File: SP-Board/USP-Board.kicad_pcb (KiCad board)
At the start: 2 copper layers, 55 x 55 mm, 8 parts, among them J10 RJ45, J11 RJ45, Q1 MMBT3906, U1 ADS1015IDGS

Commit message: Needs wires board layout 95%
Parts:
- added C1: C_Small, Capacitor_Tantalum_SMD:CP_EIA-1608-08_AVX-J_Pad1.25x1.05mm_HandSolder, B.Cu at (159.0, 107.0)
- added C2: 1uF, Capacitor_Tantalum_SMD:CP_EIA-1608-08_AVX-J_Pad1.25x1.05mm_HandSolder, B.Cu at (147.0, 95.0)
- added C3: 1uF, Capacitor_Tantalum_SMD:CP_EIA-1608-08_AVX-J_Pad1.25x1.05mm_HandSolder, B.Cu at (159.0, 98.0)
- added C4: 1uF, Capacitor_Tantalum_SMD:CP_EIA-1608-08_AVX-J_Pad1.25x1.05mm_HandSolder, B.Cu at (154.0, 98.0)
- added C5: 1uF, Capacitor_Tantalum_SMD:CP_EIA-1608-08_AVX-J_Pad1.25x1.05mm_HandSolder, B.Cu at (147.0, 89.8)
- added C6: 1uF, Capacitor_Tantalum_SMD:CP_EIA-1608-08_AVX-J_Pad1.25x1.05mm_HandSolder, B.Cu at (147.0, 85.0)
- added D1: LED, LED_SMD:LED_0603_1608Metric, F.Cu at (149.0, 110.0)
- added J1: Conn_01x02, 2.54mm_Pin_Headers:PinHeader_1x02_P2.54mm_Vertical, F.Cu at (136.0, 113.0)
- added J12: Conn_01x04, 2.54mm_Pin_Headers:PinHeader_1x04_P2.54mm_Vertical, F.Cu at (142.0, 92.0)
- added J2: Conn_01x02, 2.54mm_Pin_Headers:PinHeader_1x02_P2.54mm_Vertical, F.Cu at (136.0, 103.0)
- added J3: Conn_01x02, 2.54mm_Pin_Headers:PinHeader_1x02_P2.54mm_Vertical, F.Cu at (136.0, 108.0)
- added J4: Conn_01x02, 2.54mm_Pin_Headers:PinHeader_1x02_P2.54mm_Vertical, F.Cu at (136.0, 98.0)
- added J5: Conn_02x05_Odd_Even, Blue_ESC:Amphenol 98424-G52-10LF, F.Cu at (170.0, 89.0)
- added J6: Conn_01x03, 2.54mm_Pin_Headers:PinHeader_1x03_P2.54mm_Vertical, F.Cu at (182.0, 118.0)
- added J7: Conn_01x04, 2.54mm_Pin_Headers:PinHeader_1x04_P2.54mm_Vertical, F.Cu at (182.0, 106.0)
- added J8: Conn_01x03, 2.54mm_Pin_Headers:PinHeader_1x03_P2.54mm_Vertical, F.Cu at (177.0, 101.0)
- added J9: Conn_01x04, 2.54mm_Pin_Headers:PinHeader_1x04_P2.54mm_Vertical, F.Cu at (182.0, 111.0)
- added R1: 1k, Resistor_SMD:R_1206_3216Metric_Pad1.42x1.75mm_HandSolder, B.Cu at (142.0, 101.0)
- added R2: 27k, Resistor_SMD:R_1206_3216Metric_Pad1.42x1.75mm_HandSolder, B.Cu at (149.0, 101.0)
- added R3: 1k, Resistor_SMD:R_1206_3216Metric_Pad1.42x1.75mm_HandSolder, B.Cu at (142.0, 106.0)
- added R4: 240, Resistor_SMD:R_1206_3216Metric_Pad1.42x1.75mm_HandSolder, B.Cu at (142.0, 110.0)
- added U2: MAX232, Package_SO:SOIC-16_3.9x9.9mm_P1.27mm, B.Cu at (154.0, 90.0)
- Q1, U1: moved to B.Cu
- moved U1 14.3 mm to (159.0, 103.0), turned to 180 degrees
- moved Q1 8.41 mm to (149.0, 105.0), turned to 270 degrees
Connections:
- U1 pad 4: ANLG_Induction_SENS -> ANLG_HAL_SENS
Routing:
- net GND: track 0.00 -> 1.85 mm
- added copper zone on B.Cu, net GND

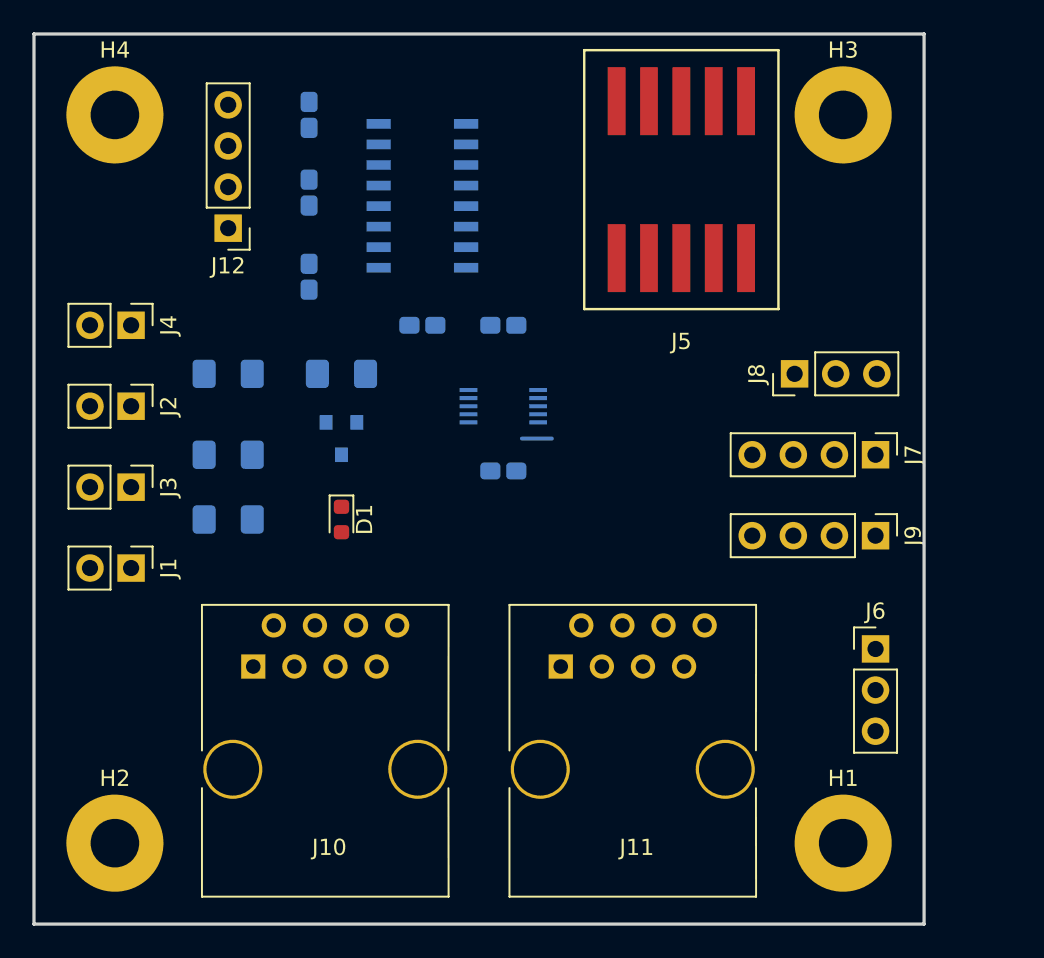
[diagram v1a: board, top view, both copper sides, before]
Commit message: added xt60
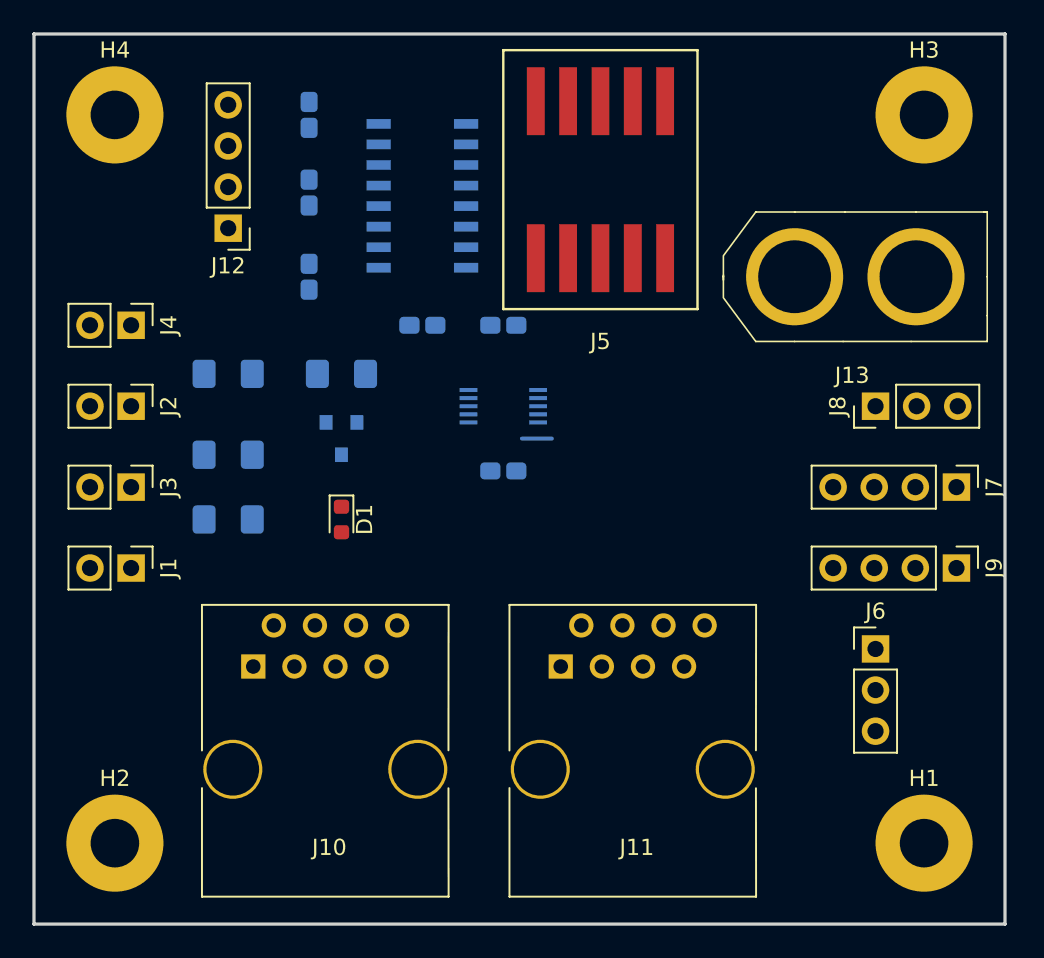
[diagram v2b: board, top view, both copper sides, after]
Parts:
- added J13: Conn_01x02, Blue_ESC:XT60, F.Cu at (177.0, 95.0)
- moved J7 5.39 mm to (187.0, 108.0)
- moved J8 5.39 mm to (182.0, 103.0)
- moved J9 5.39 mm to (187.0, 113.0)
- moved H1 5.00 mm to (185.0, 130.0)
- moved H3 5.00 mm to (185.0, 85.0)
- moved J5 5.00 mm to (165.0, 89.0)
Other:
- board size 55 x 55 mm -> 60 x 55 mm
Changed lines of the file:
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@@
     (tracks 1)
     (zones 0)
-    (modules 30)
+    (modules 31)
     (nets 43)
   )
@@
   )
   (module MountingHole:MountingHole_3mm_Pad (layer F.Cu)
-    (at 180 130)
+    (at 185 130)
     (descr "Mounting Hole 3mm")
     (tags "mounting hole 3mm")
@@
   )
   (module MountingHole:MountingHole_3mm_Pad (layer F.Cu)
-    (at 180 85)
+    (at 185 85)
     (descr "Mounting Hole 3mm")
     (tags "mounting hole 3mm")
@@
   )
   (module "Blue_ESC:Amphenol 98424-G52-10LF" (layer F.Cu)
-    (at 170 89)
+    (at 165 89)
     (fp_text reference J5 (at 0 10) (layer F.SilkS)
       (effects (font (size 1 1) (thickness 0.15)))
@@
   )
   (module 2.54mm_Pin_Headers:PinHeader_1x04_P2.54mm_Vertical (layer F.Cu)
-    (at 182 106 270)
+    (at 187 108 270)
     (descr "Through hole straight pin header, 1x04, 2.54mm pitch, single row")
     (tags "Through hole pin header THT 1x04 2.54mm single row")
@@
   )
   (module 2.54mm_Pin_Headers:PinHeader_1x03_P2.54mm_Vertical (layer F.Cu)
-    (at 177 101 90)
+    (at 182 103 90)
     (descr "Through hole straight pin header, 1x03, 2.54mm pitch, single row")
     (tags "Through hole pin header THT 1x03 2.54mm single row")
@@
   )
   (module 2.54mm_Pin_Headers:PinHeader_1x04_P2.54mm_Vertical (layer F.Cu)
-    (at 182 111 270)
+    (at 187 113 270)
     (descr "Through hole straight pin header, 1x04, 2.54mm pitch, single row")
     (tags "Through hole pin header THT 1x04 2.54mm single row")
@@
     )
   )
+  (module Blue_ESC:XT60 (layer F.Cu)
+    (at 177 95)
+    (fp_text reference J13 (at 3.556 6.096) (layer F.SilkS)
+      (effects (font (size 1 1) (thickness 0.15)))
+    )
+    (fp_text value Conn_01x02 (at 3.2 -5.9) (layer F.Fab)
+      (effects (font (size 1 1) (thickness 0.15)))
+    )
+    (fp_line (start 7.2 4) (end 11.9 4) (layer F.SilkS) (width 0.1))
+    (fp_line (start 11.9 4) (end 11.9 2.4) (layer F.SilkS) (width 0.1))
+    (fp_line (start 7.5 -4) (end 11.7 -4) (layer F.SilkS) (width 0.1))
+    (fp_line (start 11.7 -4) (end 11.8 -4) (layer F.SilkS) (width 0.1))
+    (fp_line (start 11.8 -4) (end 11.9 -4) (layer F.SilkS) (width 0.1))
+    (fp_line (start 11.9 -4) (end 11.9 0) (layer F.SilkS) (width 0.1))
+    (fp_line (start -2.4 4) (end -4.4 1.3) (layer F.SilkS) (width 0.1))
+    (fp_line (start -2.4 -4) (end -4.4 -1.3) (layer F.SilkS) (width 0.1))
+    (fp_line (start -4.4 0) (end -4.4 1.25) (layer F.SilkS) (width 0.1))
+    (fp_line (start -4.4 0) (end -4.4 -1.25) (layer F.SilkS) (width 0.1))
+    (fp_line (start 0 4) (end -2.4 4) (layer F.SilkS) (width 0.1))
+    (fp_line (start 3 4) (end 0 4) (layer F.SilkS) (width 0.1))
+    (fp_line (start 0 -4) (end -2.4 -4) (layer F.SilkS) (width 0.1))
+    (fp_line (start 3.1 -4) (end 0 -4) (layer F.SilkS) (width 0.1))
+    (fp_line (start -4.4 -0.1) (end -4.4 0.2) (layer F.SilkS) (width 0.1))
+    (fp_line (start 11.9 0) (end 11.9 2.4) (layer F.SilkS) (width 0.1))
+    (fp_line (start 7.5 -4) (end 3.1 -4) (layer F.SilkS) (width 0.1))
+    (fp_line (start 7.2 4) (end 3 4) (layer F.SilkS) (width 0.1))
+    (pad 1 thru_hole circle (at 0 0) (size 6 6) (drill 4.5) (layers *.Cu *.Mask F.SilkS)
+      (net 6 GND))
+    (pad 2 thru_hole circle (at 7.5 0) (size 6 6) (drill 4.5) (layers *.Cu *.Mask F.SilkS)
+      (net 35 +12V))
+  )
   (gr_line (start 130 135) (end 130 80) (layer Edge.Cuts) (width 0.2))
-  (gr_line (start 185 135) (end 130 135) (layer Edge.Cuts) (width 0.2))
-  (gr_line (start 185 80) (end 185 135) (layer Edge.Cuts) (width 0.2))
-  (gr_line (start 130 80) (end 185 80) (layer Edge.Cuts) (width 0.2))
+  (gr_line (start 190 135) (end 130 135) (layer Edge.Cuts) (width 0.2))
+  (gr_line (start 190 80) (end 190 135) (layer Edge.Cuts) (width 0.2))
+  (gr_line (start 130 80) (end 190 80) (layer Edge.Cuts) (width 0.2))
   (segment (start 160.15 105) (end 162 105) (width 0.25) (layer B.Cu) (net 6))
   (zone (net 6) (net_name GND) (layer B.Cu) (hatch edge 0.508)
@@
     (polygon
       (pts
-        (xy 130 135) (xy 185 135) (xy 185 80) (xy 130 80)
+        (xy 130 135) (xy 190 135) (xy 190 80) (xy 130 80)
       )
     )

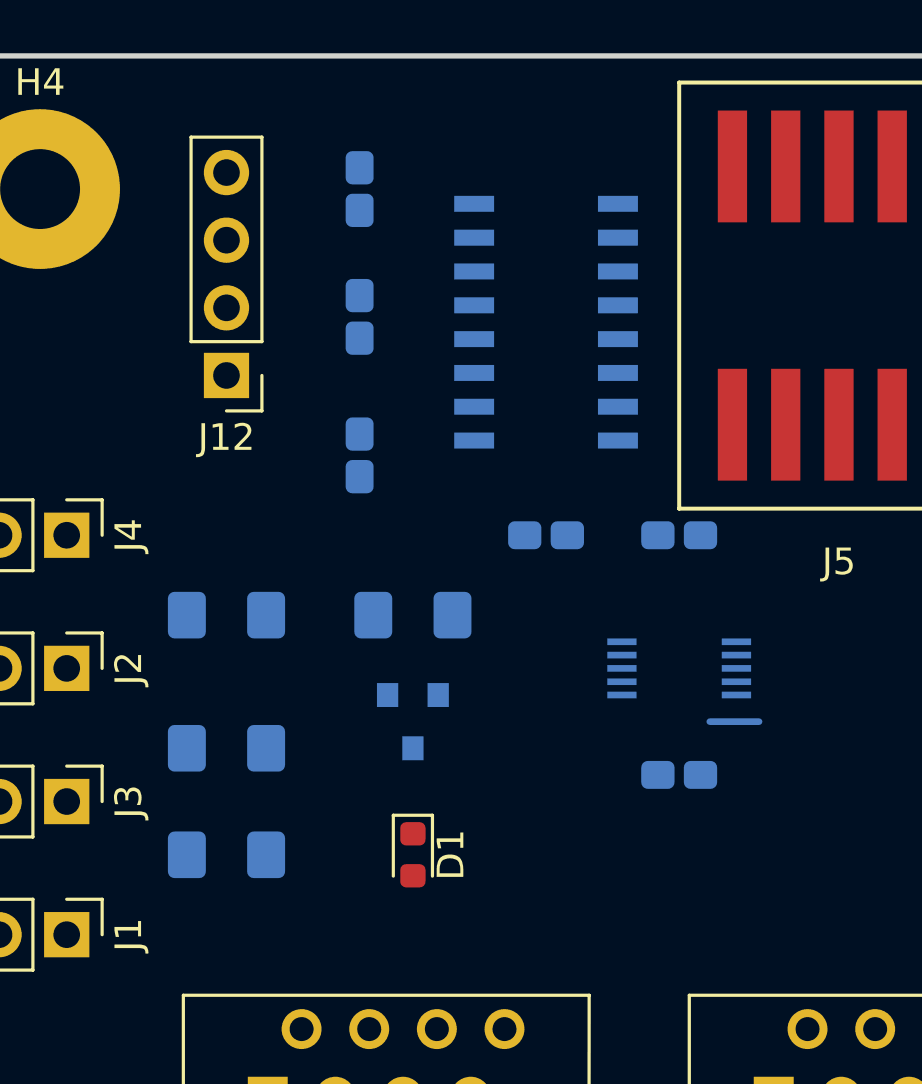
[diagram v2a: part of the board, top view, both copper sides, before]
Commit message: com board prelim is finaly done
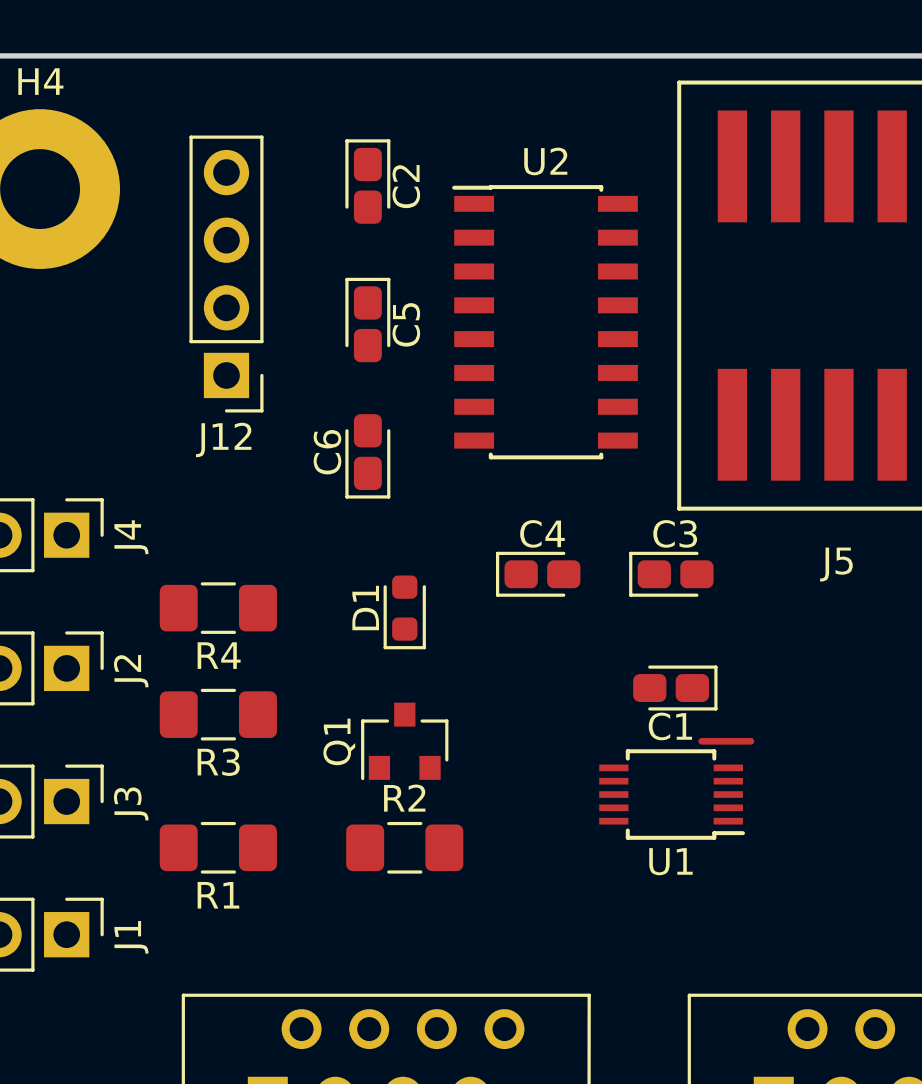
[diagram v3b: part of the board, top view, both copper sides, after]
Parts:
- C1, C2, C3, C4, C5, C6, Q1, R1, R2, R3, R4, U1, U2: moved to F.Cu
- moved C2 10.1 mm to (147.3, 84.9), turned to 270 degrees
- moved C6 9.88 mm to (147.3, 94.9), turned to 90 degrees
- moved D1 9.27 mm to (148.7, 100.7), turned to 90 degrees
- moved R4 9.27 mm to (141.7, 100.7)
- moved R1 8.74 mm to (141.7, 109.7)
- moved R2 8.74 mm to (148.7, 109.7)
- moved U1 4.75 mm to (158.7, 107.7)
- moved C1 3.28 mm to (158.7, 103.7)
- moved C3 1.47 mm to (158.9, 99.5)
- moved C4 1.47 mm to (153.9, 99.5)
- moved R3 1.30 mm to (141.7, 104.7)
- moved Q1 0.80 mm to (148.7, 105.7), turned to 90 degrees
- moved C5 0.42 mm to (147.3, 90.1), turned to 270 degrees

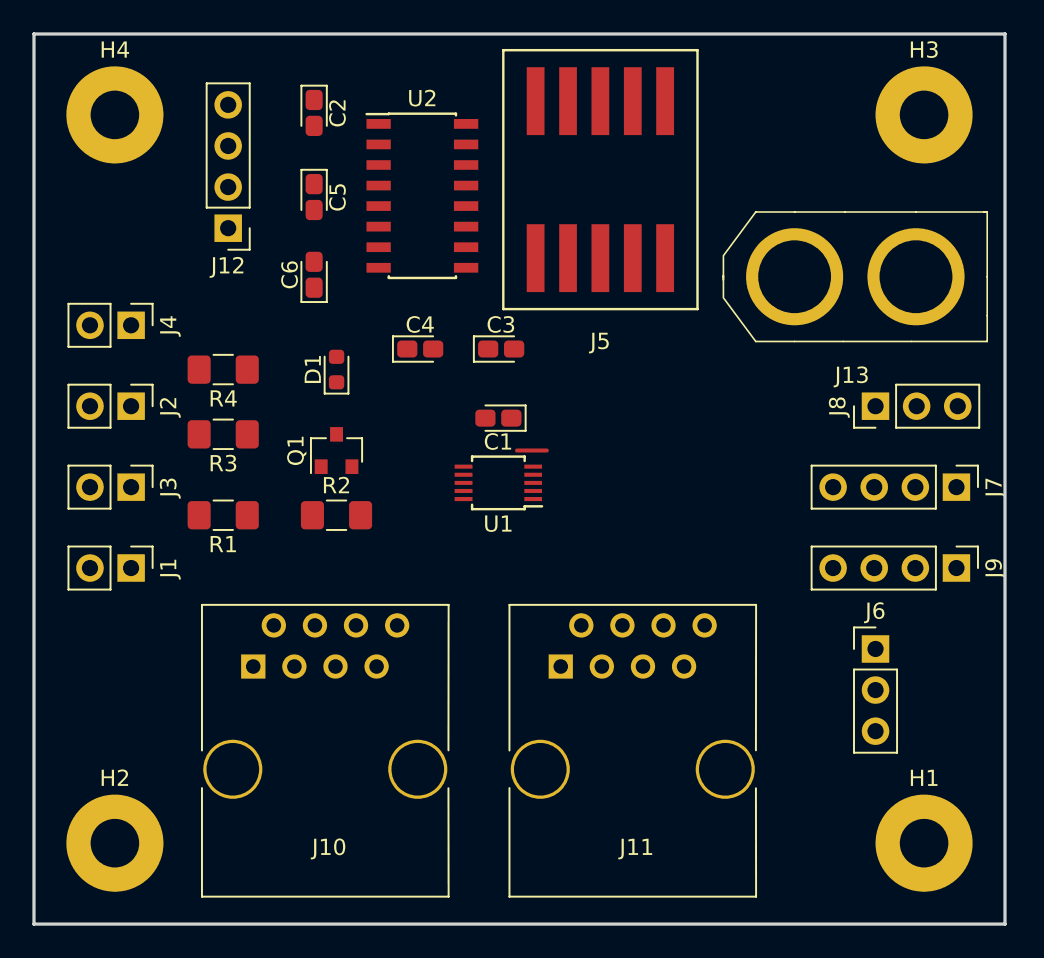
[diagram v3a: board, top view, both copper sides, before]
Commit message: wiring done
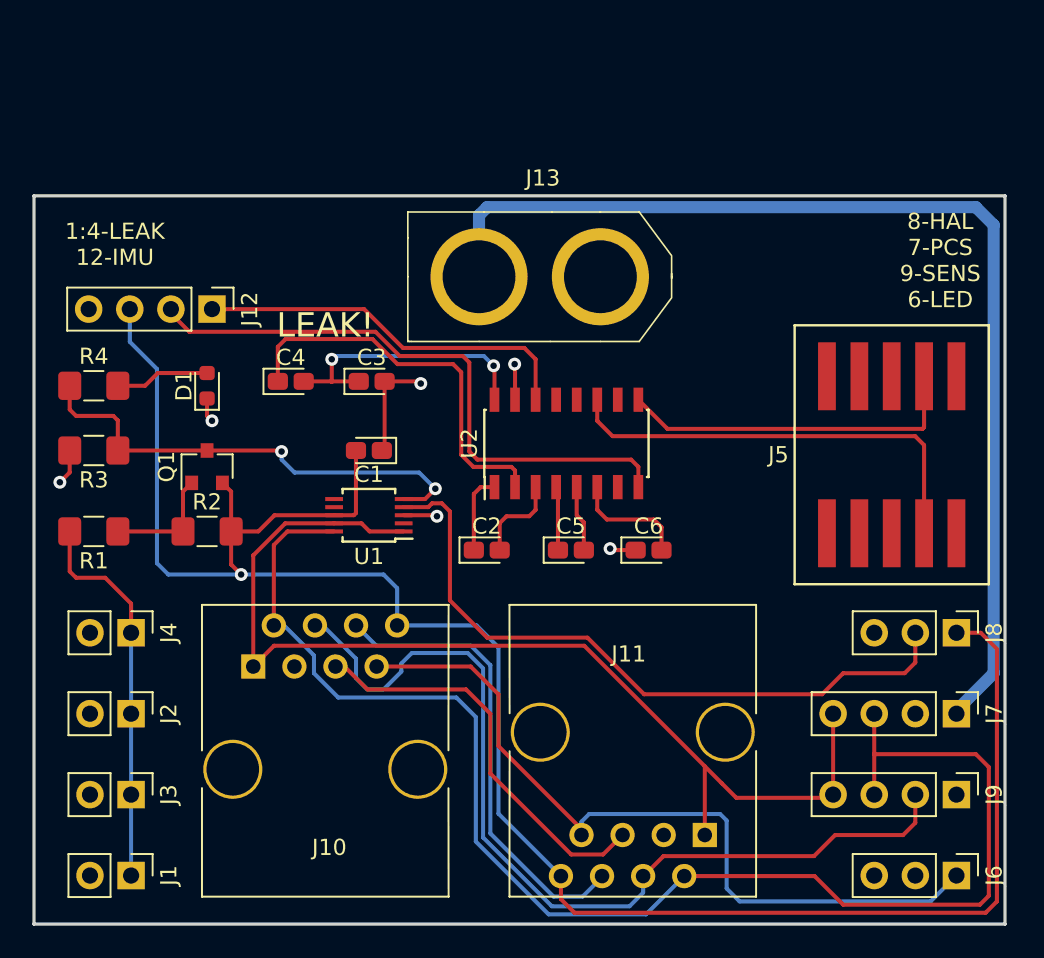
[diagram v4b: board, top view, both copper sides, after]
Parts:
- removed H1, H2, H3, H4: MountingHole, MountingHole:MountingHole_3mm_Pad
- moved C2 29.0 mm to (158.0, 111.9), turned to 0 degrees
- moved C5 27.0 mm to (163.2, 111.9), turned to 0 degrees
- moved C6 26.8 mm to (168.0, 111.9), turned to 0 degrees
- moved J5 24.8 mm to (183.0, 106.0), turned to 180 degrees
- moved J1 19.0 mm to (136.0, 132.0)
- moved J2 19.0 mm to (136.0, 122.0)
- moved J3 19.0 mm to (136.0, 127.0)
- moved J4 19.0 mm to (136.0, 117.0)
- moved U2 17.7 mm to (162.9, 105.3), turned to 90 degrees
- moved J6 14.9 mm to (187.0, 132.0), turned to 270 degrees
- moved J8 14.9 mm to (187.0, 117.0), turned to 270 degrees
- moved J7 14.0 mm to (187.0, 122.0)
- moved J9 14.0 mm to (187.0, 127.0)
- moved J13 12.0 mm to (165.0, 95.0), turned to 180 degrees
- moved C1 8.25 mm to (150.7, 105.7)
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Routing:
- net +5V: track 0.00 -> 122.4 mm, vias 0 -> 1
- net I2C_SCL: track 0.00 -> 88.1 mm
- net +12V: track 0.00 -> 67.4 mm
- net I2C_SDA: track 0.00 -> 66.8 mm
- net +3V3: track 0.00 -> 57.7 mm
- net EXT_PWM_LED: track 0.00 -> 48.6 mm
- net ANLG_HAL_SENS: track 0.00 -> 42.5 mm
- net Net-(J12-Pad2): track 0.00 -> 37.6 mm
- net Leak_Sig: track 0.00 -> 29.7 mm, vias 0 -> 2
- net EXT_Temp_1: track 0.00 -> 28.8 mm
- net Net-(J5-Pad7): track 0.00 -> 27.6 mm
- net EXT_Temp_0: track 0.00 -> 25.2 mm
- net Net-(C4-Pad1): track 0.00 -> 24.4 mm
- net Leak_Probe: track 0.00 -> 23.9 mm
- net Net-(J12-Pad1): track 0.00 -> 23.8 mm
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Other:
- board size 60 x 55 mm -> 60 x 45 mm
- net class 12v added: clearance 0.2, trace_width 0.75, via_dia 0.8, via_drill 0.4
- board text added: "1:4-LEAK 12-IMU"
- board text added: "8-HAL 7-PCS 9-SENS 6-LED"
- board text added: "LEAK!"
